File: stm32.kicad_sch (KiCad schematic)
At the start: 48 parts, among them J1 USB_B_Micro, J19 Conn_01x06, J2 Conn_02x05_Odd_Even, J7 TC2030, SW1 SW_Push, SW2 SW_Push, SW3 SW_Push, SW4 SW_Push, U1 STM32F427VGT6, U3 molex_48pin_MRE, U5 LM1117-3.3, X1 8MHz 20pF, Y2 32768 Hz

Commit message: First commit
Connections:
- net 5V: now also U3.J201, U3.J202
- net GND: now also U3.J207, U3.J208, U3.J32
- net NRST: now also U3.J210
- net PA13: now also U3.J209
- net PA14: now also U3.J205
- net PB3: now also U3.J206
- net VDD: now also U3.J203, U3.J204
- net Vrtc: now also U3.J31

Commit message: did stuff
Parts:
- U3: footprint (none) -> rusefi_lib:Molex_48_BCM
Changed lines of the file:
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@@
       (effects (font (size 1.524 1.524)) (justify left) hide)
     )
-    (property "Footprint" "" (id 2) (at 140.97 78.105 0)
+    (property "Footprint" "rusefi_lib:Molex_48_BCM" (id 2) (at 140.97 78.105 0)
       (effects (font (size 1.524 1.524)) hide)
     )
@@
       (effects (font (size 1.524 1.524)) hide)
     )
-    (property "Footprint" "" (id 2) (at 323.85 165.1 0)
+    (property "Footprint" "rusefi_lib:Molex_48_BCM" (id 2) (at 323.85 165.1 0)
       (effects (font (size 1.524 1.524)) hide)
     )

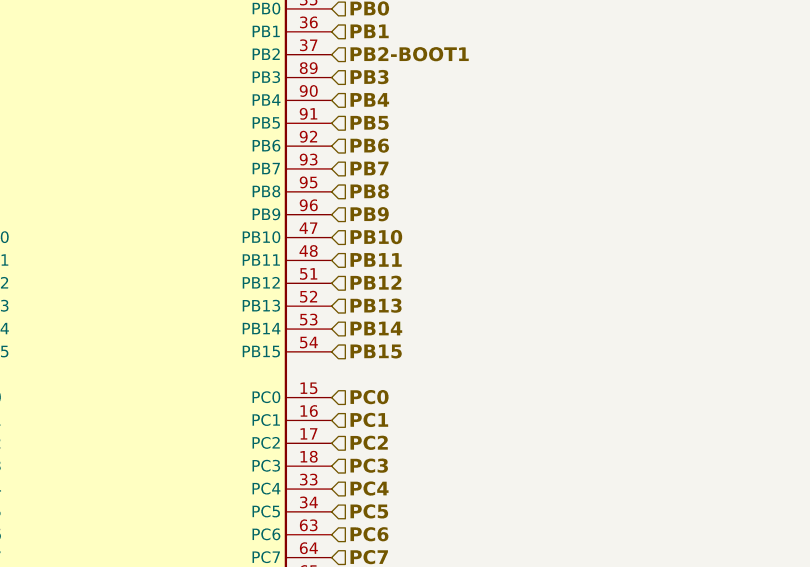
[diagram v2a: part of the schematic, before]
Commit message: Fixed CAN and 5v pads
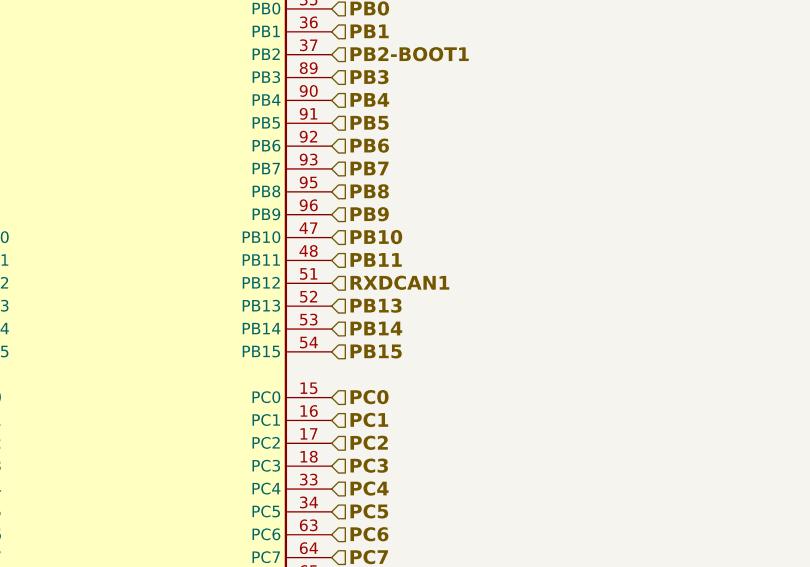
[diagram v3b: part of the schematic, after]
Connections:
- net PB12 renamed RXDCAN1
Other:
- title: microRusEFI-2L -> MRE IO Expander
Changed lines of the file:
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@@
   (paper "B")
   (title_block
-    (title "microRusEFI-2L")
-    (date "2020-05-24")
-    (rev "R0.5.2")
+    (title "MRE IO Expander")
+    (date "2021-02-")
+    (rev "R0.1")
     (company "rusEFI.com")
-    (comment 1 "Donald Becker")
+    (comment 1 "Simon Orchard")
     (comment 2 "AI6OD")
   )
@@
     (effects (font (size 1.524 1.524) (thickness 0.3048) bold) (justify left))
   )
-  (hierarchical_label "PB12" (shape input) (at 186.69 171.45 0)
-    (effects (font (size 1.524 1.524) (thickness 0.3048) bold) (justify left))
-  )
+  (hierarchical_label "RXDCAN1" (shape input) (at 186.69 171.45 0)
+    (effects (font (size 1.524 1.524) (thickness 0.3048) bold) (justify left))
+  )

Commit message: Work on 6 axis
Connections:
- net PA14: now also U1.89 (PB3)
- net PB3: no longer U1.89 (PB3)
- net PB4 renamed SDO
- net PB5 renamed SDI
- net PE15 renamed CS
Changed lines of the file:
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@@
     (effects (font (size 1.524 1.524) (thickness 0.3048) bold) (justify left))
   )
-  (hierarchical_label "PB3" (shape input) (at 186.69 148.59 0)
+  (hierarchical_label "SCK" (shape input) (at 186.69 148.59 0)
     (effects (font (size 1.524 1.524) (thickness 0.3048) bold) (justify left))
   )
@@
     (effects (font (size 1.524 1.524) (thickness 0.3048) bold) (justify right))
   )
-  (hierarchical_label "PE15" (shape input) (at 140.97 179.07 180)
+  (hierarchical_label "CS" (shape input) (at 140.97 179.07 180)
     (effects (font (size 1.524 1.524) (thickness 0.3048) bold) (justify right))
   )
@@
     (effects (font (size 1.524 1.524) (thickness 0.3048) bold) (justify left))
   )
-  (hierarchical_label "PB5" (shape input) (at 186.69 153.67 0)
+  (hierarchical_label "SDI" (shape input) (at 186.69 153.67 0)
     (effects (font (size 1.524 1.524) (thickness 0.3048) bold) (justify left))
   )
@@
     (effects (font (size 1.524 1.524) (thickness 0.3048) bold) (justify left))
   )
-  (hierarchical_label "PB4" (shape input) (at 186.69 151.13 0)
+  (hierarchical_label "SDO" (shape input) (at 186.69 151.13 0)
     (effects (font (size 1.524 1.524) (thickness 0.3048) bold) (justify left))
   )
